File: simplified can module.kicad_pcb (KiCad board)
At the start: 2 copper layers, 28.4 x 20.3 mm, 18 parts, among them J1 Conn_01x07_Pin, J2 SCREW-TERMINAL-2P'5.08', U1 MCP2517FD, U2 MCP2542, X1 20MHz

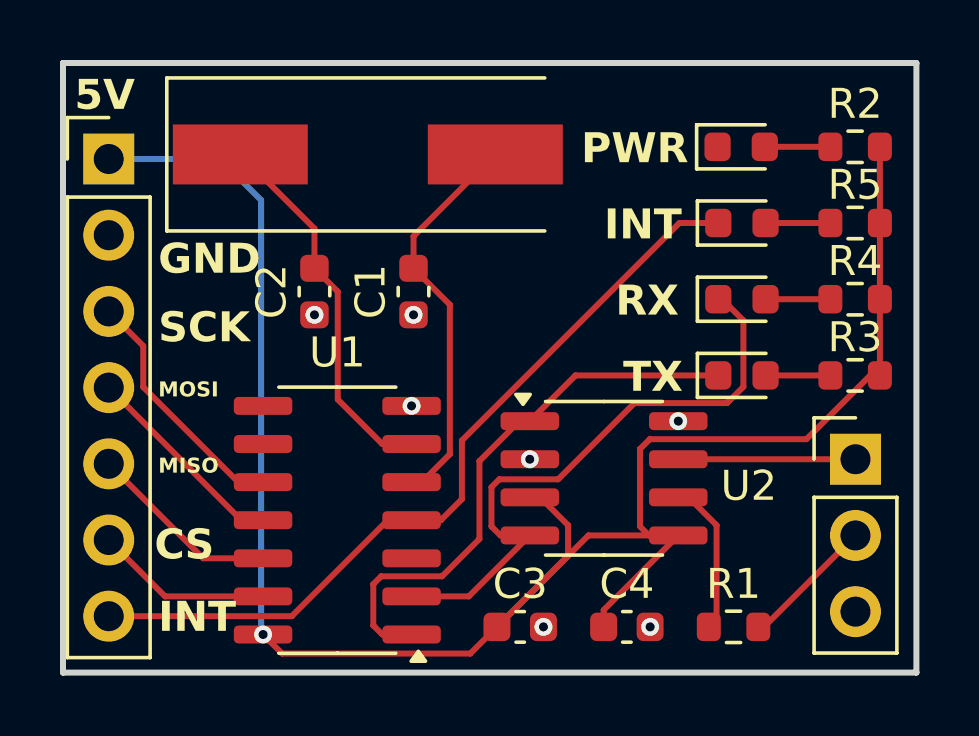
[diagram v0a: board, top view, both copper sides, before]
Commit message: add CAN pin labels
also:
- reduced thermal relief spoke size to help soldering
- changed solder mask color to purple in 3d renderer
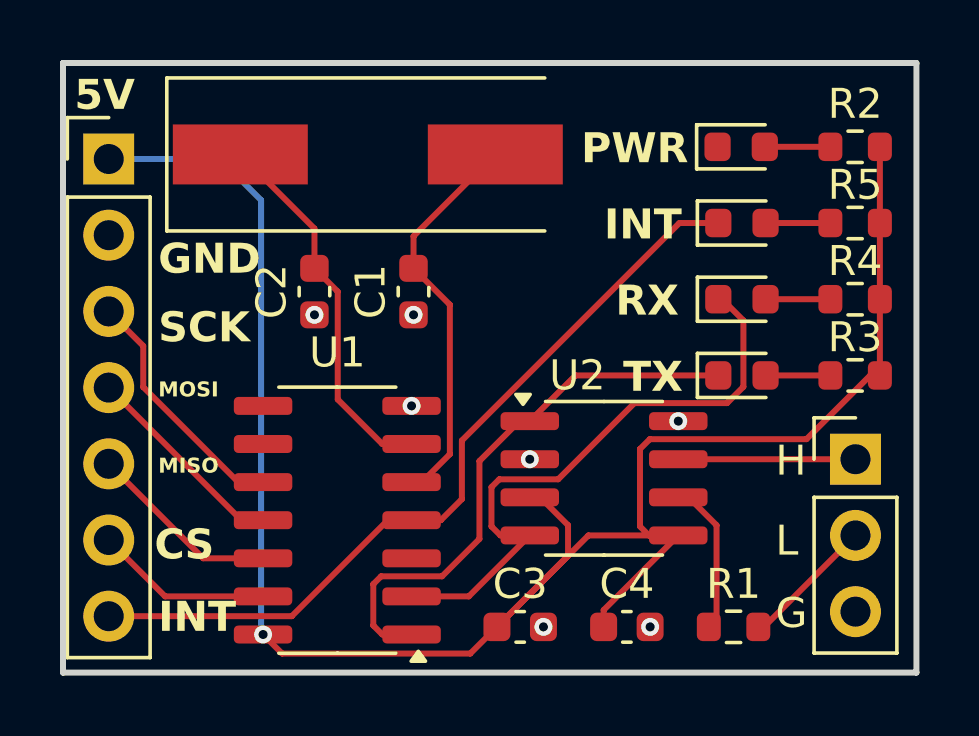
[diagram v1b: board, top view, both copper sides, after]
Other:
- board text added: "G"
- board text added: "H"
- board text added: "L"
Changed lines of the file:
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@@
 			(pinfunction "K")
 			(pintype "passive")
+			(thermal_bridge_width 0.3)
 		)
 		(pad "2" smd roundrect
@@
 		(tags "SOIC SO")
 		(property "Reference" "U2"
-			(at 4.826 0.254 0)
+			(at -0.889 -3.429 0)
 			(layer "F.SilkS")
 			(effects
@@
 		)
 	)
+	(gr_text "L"
+		(at 141.605 90.17 0)
+		(layer "F.SilkS")
+		(effects
+			(font
+				(size 1 1)
+				(thickness 0.15)
+			)
+			(justify left bottom)
+		)
+	)
 	(gr_text "MISO"
 		(at 121.031 87.376 0)
@@
 		)
 	)
+	(gr_text "G"
+		(at 141.605 92.583 0)
+		(layer "F.SilkS")
+		(effects
+			(font
+				(size 1 1)
+				(thickness 0.15)
+			)
+			(justify left bottom)
+		)
+	)
 	(gr_text "INT"
 		(at 135.89 79.629 0)
@@
 		)
 	)
+	(gr_text "H"
+		(at 141.605 87.503 0)
+		(layer "F.SilkS")
+		(effects
+			(font
+				(size 1 1)
+				(thickness 0.15)
+			)
+			(justify left bottom)
+		)
+	)
 	(gr_text "MOSI"
 		(at 121.031 84.836 0)
@@
 		(fill yes
 			(thermal_gap 0.5)
-			(thermal_bridge_width 0.5)
+			(thermal_bridge_width 0.3)
 		)
 		(polygon

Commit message: update CAN header labels
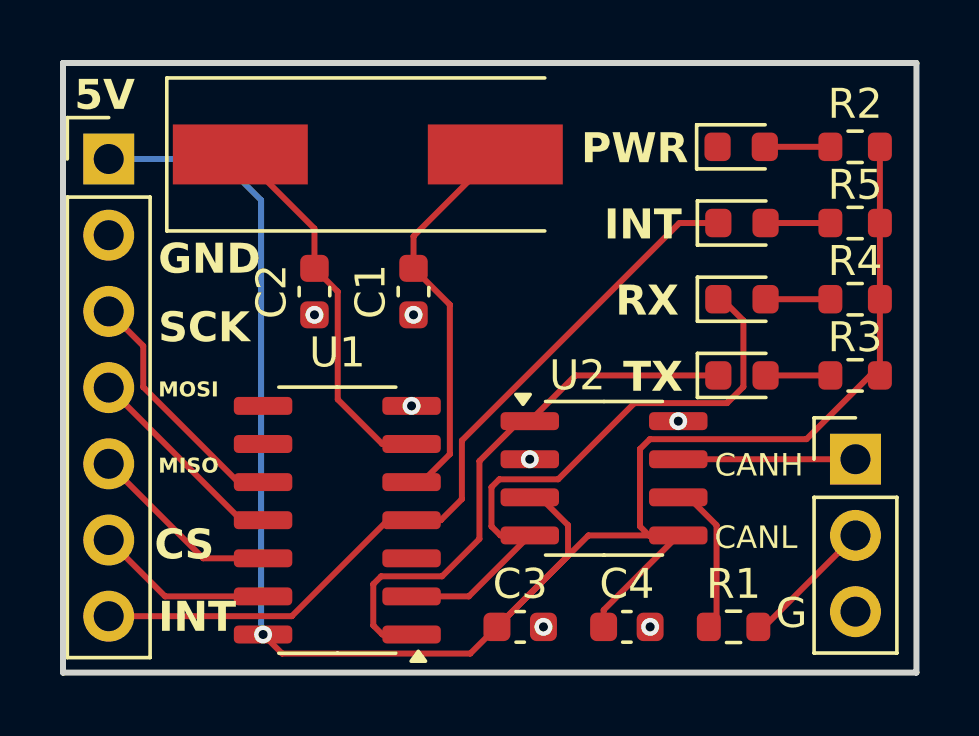
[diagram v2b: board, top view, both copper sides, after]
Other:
- board text added: "CANH"
- board text added: "CANL"
- board text removed: "H"
- board text removed: "L"
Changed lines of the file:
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@@
-		)
-	)
-	(gr_text "L"
-		(at 141.605 90.17 0)
-		(layer "F.SilkS")
-		(effects
-			(font
-				(size 1 1)
-				(thickness 0.15)
-			)
-			(justify left bottom)
 		)
 	)
@@
 		)
 	)
+	(gr_text "CANL"
+		(at 139.573 89.916 0)
+		(layer "F.SilkS")
+		(effects
+			(font
+				(size 0.75 0.75)
+				(thickness 0.15)
+			)
+			(justify left bottom)
+		)
+	)
 	(gr_text "RX"
 		(at 136.271 82.169 0)
@@
 		)
 	)
-	(gr_text "H"
-		(at 141.605 87.503 0)
+	(gr_text "CANH"
+		(at 139.573 87.503 0)
 		(layer "F.SilkS")
 		(effects
 			(font
-				(size 1 1)
+				(size 0.75 0.75)
 				(thickness 0.15)
 			)

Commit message: add copyright and version info
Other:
- board text added: "spicanfd r1.1 copyright (c) 2025 Eli Rutan"
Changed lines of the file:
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@@
+		)
+	)
+	(gr_text "spicanfd r1.1\ncopyright (c) 2025 Eli Rutan"
+		(at 133.096 82.169 0)
+		(layer "B.SilkS")
+		(effects
+			(font
+				(size 1 1)
+				(thickness 0.1)
+			)
+			(justify bottom mirror)
 		)
 	)
